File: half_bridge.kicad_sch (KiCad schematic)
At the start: 26 parts, among them Q11 BC817, Q12 NMOS, Q13 BC817, Q14 BC807, Q15 BC817, Q16 BC817, Q17 NMOS, Q18 BC817, Q19 BC807, Q20 BC817

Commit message: foi adicionado o arduino e conector de encoder na mesma placa, utilizando optacopladores recomeço do layout pcb
 Changes to be committed:
	new file:   controle.kicad_sch
	modified:   dc_converter_sch.kicad_sch
	modified:   half_bridge.kicad_sch
	modified:   volante.kicad_pcb
	modified:   volante.kicad_prl
	modified:   volante.kicad_pro
	modified:   volante.kicad_sch
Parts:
- R12, R14, R16, R17, R18: footprint (none) -> PCM_SparkFun-Resistor:R_0805_2012Metric
- R13: footprint (none) -> PCM_SparkFun-Resistor:R_1206_3216Metric

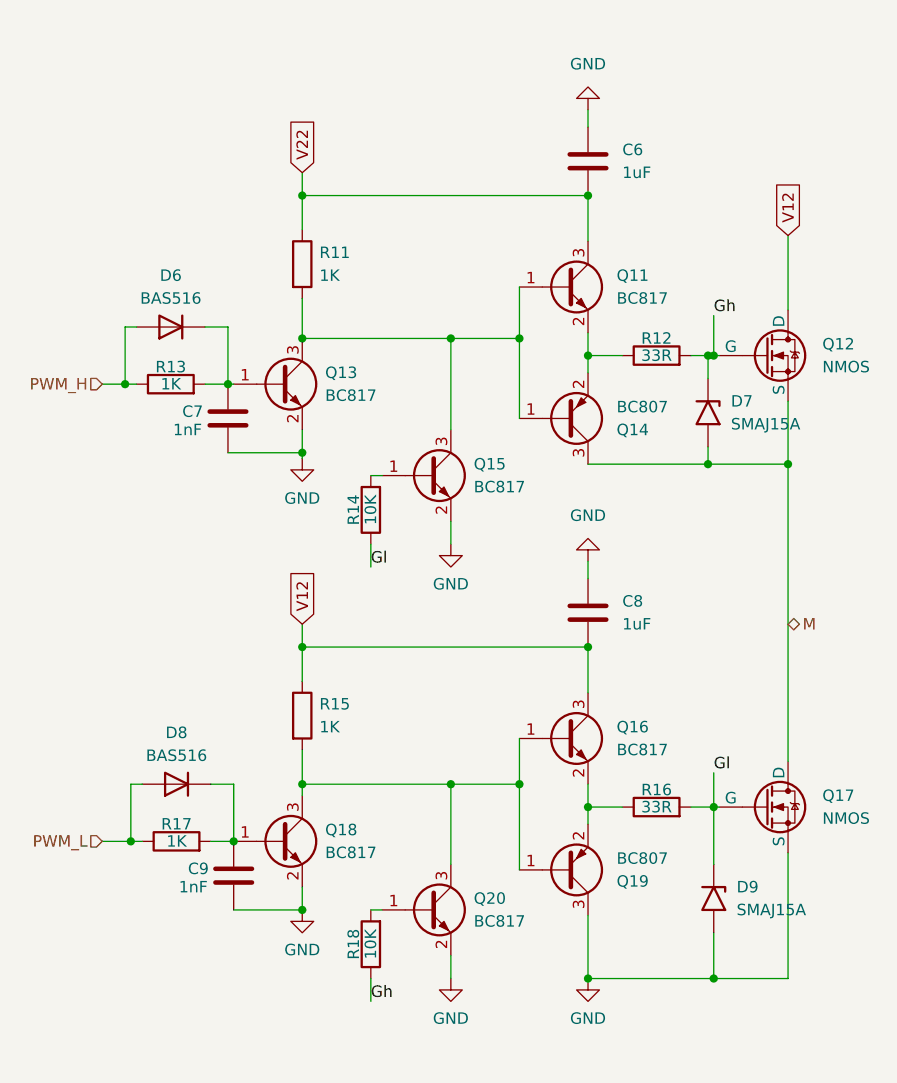
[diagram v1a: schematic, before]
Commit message: alteração no circuito de controle: adição dos isoladores
  Changes to be committed:
 	new file:   .history
 	modified:   controle.kicad_sch
 	modified:   dc_converter_sch.kicad_sch
 	modified:   h_bridge_sch.kicad_sch
 	modified:   half_bridge.kicad_sch
 	modified:   volante.kicad_pcb
 	modified:   volante.kicad_prl
 	modified:   volante.kicad_pro
 	modified:   volante.kicad_sch

  Changes not staged for commit:
 	modified:   .history (modified content, untracked content)
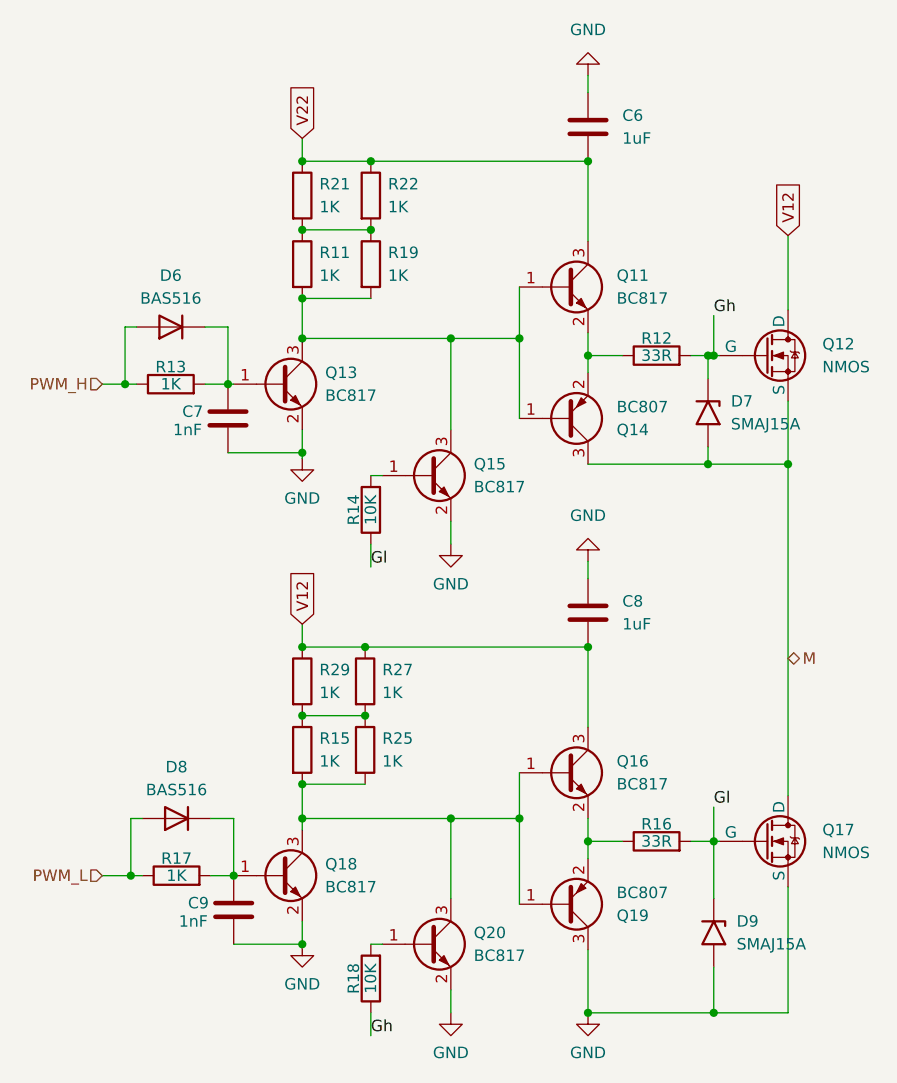
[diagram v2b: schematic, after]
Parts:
- added R19, R21, R22, R25, R27, R29: 1K, Resistor_THT:R_Axial_DIN0207_L6.3mm_D2.5mm_P2.54mm_Vertical, symbol Device:R
- R11, R15: footprint (none) -> Resistor_THT:R_Axial_DIN0207_L6.3mm_D2.5mm_P2.54mm_Vertical
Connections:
- net V12: now also R27.1, R29.1; no longer R15.1
- net V22: now also R21.1, R22.1; no longer R11.1
- net at Q11.1 (B), Q13.3 (C), Q14.1 (B)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: now also R19.2
- net at Q16.1 (B), Q18.3 (C), Q19.1 (B)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: now also R25.2
- new net: R11.1, R19.1, R21.2, R22.2
- new net: R15.1, R25.1, R27.2, R29.2
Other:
- moved on the sheet: C6, C9, D8, D9, Q16, Q17, Q18, Q19, Q20, R15, R16, R17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
